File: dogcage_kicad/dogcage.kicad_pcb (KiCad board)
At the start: 2 copper layers, 68.6 x 49.8 mm, 17 parts, among them CON1 5V, M1 XBEE, P1 Door, P2 Servo, P3 CONN_01X10, P4 CONN_01X10, P5 CONN_01X14, P7 CONN_01X14, Q1 TIP120, SW1 SW_PUSH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

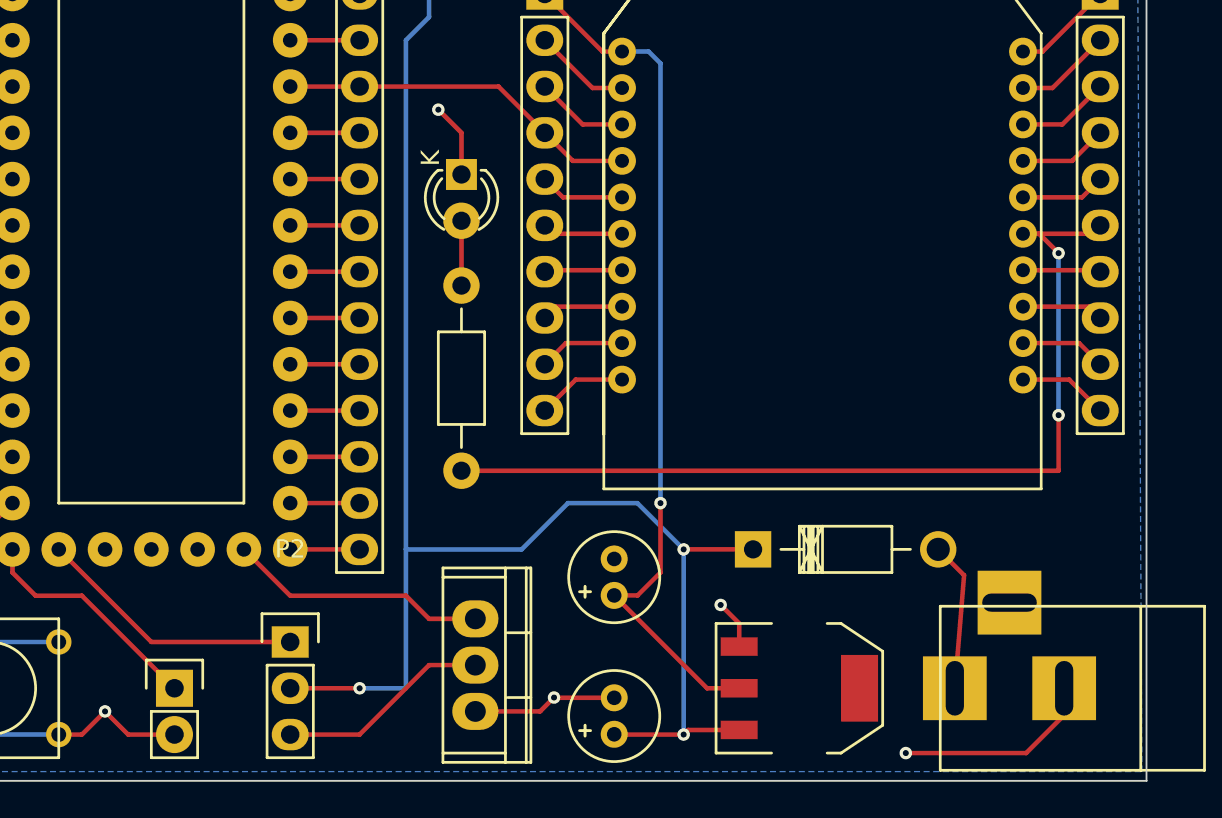
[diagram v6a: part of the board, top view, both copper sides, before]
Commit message: Fixed front silkscreen, added name/email to back
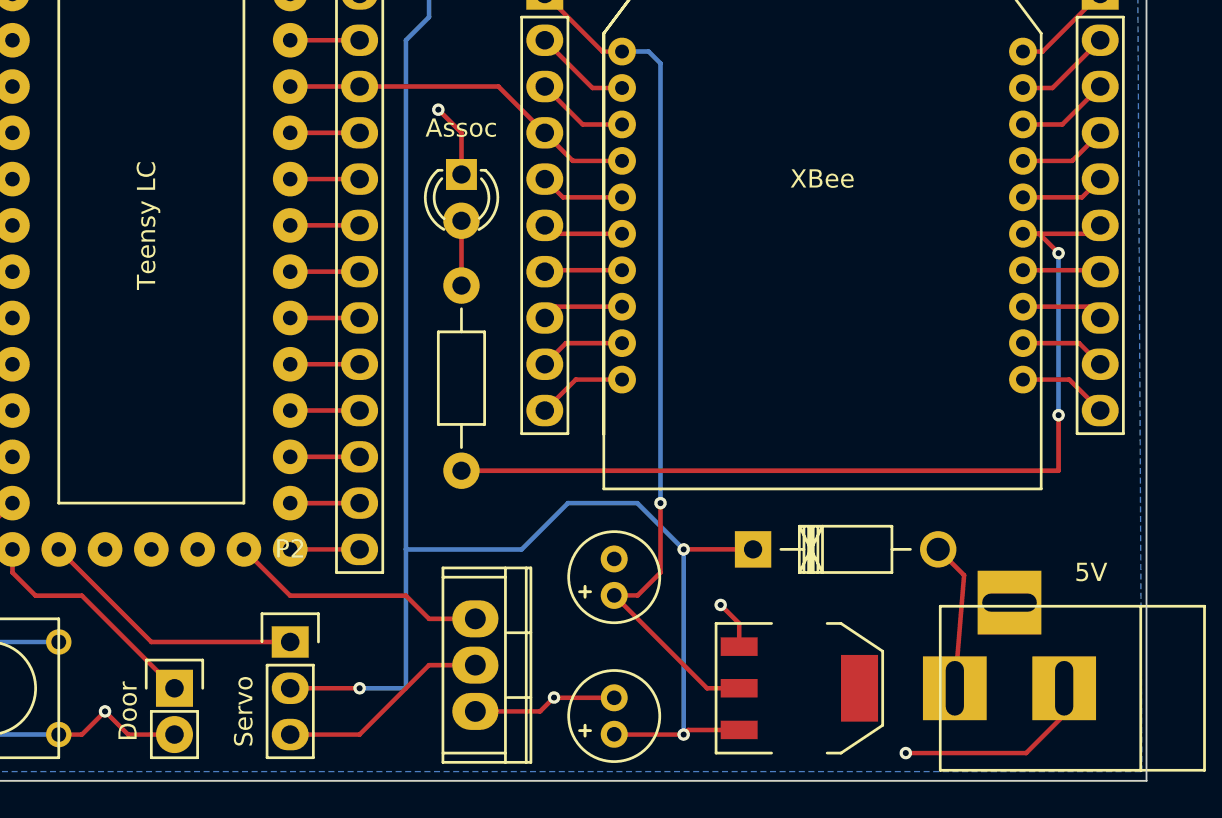
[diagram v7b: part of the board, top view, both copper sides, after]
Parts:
- M1: value XBEE -> XBee
- U2: value TEENSYLC -> Teensy LC
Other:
- board text added: "https://github.com/tpmanley/dogcage Tom Manley tom.manley@gmail.com"
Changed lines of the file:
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@@
     (area 126.971667 123.315 201.577621 175.310001)
     (thickness 1.6)
-    (drawings 4)
+    (drawings 5)
     (tracks 157)
     (zones 0)
@@
     (0 F.Cu signal)
     (31 B.Cu signal)
-    (32 B.Adhes user)
-    (33 F.Adhes user)
-    (34 B.Paste user)
-    (35 F.Paste user)
     (36 B.SilkS user)
     (37 F.SilkS user)
     (38 B.Mask user)
     (39 F.Mask user)
-    (40 Dwgs.User user)
-    (41 Cmts.User user)
-    (42 Eco1.User user)
-    (43 Eco2.User user)
     (44 Edge.Cuts user)
-    (45 Margin user)
-    (46 B.CrtYd user)
-    (47 F.CrtYd user)
-    (48 B.Fab user)
-    (49 F.Fab user)
   )
   (setup
@@
     (visible_elements FFFFFF7F)
     (pcbplotparams
-      (layerselection 0x00030_80000001)
-      (usegerberextensions false)
+      (layerselection 0x010f0_80000001)
+      (usegerberextensions true)
       (excludeedgelayer true)
       (linewidth 0.100000)
@@
       (outputformat 1)
       (mirror false)
-      (drillshape 1)
+      (drillshape 0)
       (scaleselection 1)
-      (outputdirectory ""))
+      (outputdirectory gerbers/))
   )
   (net 0 "")
@@
       (effects (font (size 1 1) (thickness 0.15)))
     )
-    (fp_text value 5V (at -1.27 6.35 180) (layer F.Fab)
+    (fp_text value 5V (at -1.27 6.35 180) (layer F.SilkS)
       (effects (font (size 1 1) (thickness 0.15)))
     )
@@
       (effects (font (size 1 1) (thickness 0.15)))
     )
-    (fp_text value Assoc (at -2.54 0 360) (layer F.Fab)
+    (fp_text value Assoc (at -2.54 0 360) (layer F.SilkS)
       (effects (font (size 1 1) (thickness 0.15)))
     )
@@
     (fp_arc (start 1.28 0) (end 3.02 0.96) (angle 110) (layer F.SilkS) (width 0.15))
     (fp_arc (start 1.27 0) (end 2.44 0.94) (angle 95.5) (layer F.SilkS) (width 0.15))
-    (fp_text user K (at -0.9 1.7 270) (layer F.SilkS)
+    (fp_text user K (at -0.9 1.7 270) (layer F.SilkS) hide
       (effects (font (size 1 1) (thickness 0.15)))
     )
@@
       (effects (font (size 1 1) (thickness 0.15)))
     )
-    (fp_text value XBEE (at 0 0) (layer F.Fab) hide
+    (fp_text value XBee (at 0 0) (layer F.SilkS)
       (effects (font (size 1 1) (thickness 0.15)))
     )
@@
       (effects (font (size 1 1) (thickness 0.15)))
     )
-    (fp_text value Door (at -2.54 1.27 90) (layer F.Fab)
+    (fp_text value Door (at -2.54 1.27 90) (layer F.SilkS)
       (effects (font (size 1 1) (thickness 0.15)))
     )
@@
       (effects (font (size 1 1) (thickness 0.15)))
     )
-    (fp_text value Servo (at -2.54 3.81 90) (layer F.Fab)
+    (fp_text value Servo (at -2.54 3.81 90) (layer F.SilkS)
       (effects (font (size 1 1) (thickness 0.15)))
     )
@@
     (fp_line (start 2.032 -4.572) (end 3.556 -2.286) (layer F.SilkS) (width 0.15))
     (fp_line (start 3.556 -2.286) (end 3.556 -1.524) (layer F.SilkS) (width 0.15))
-    (pad 4 smd rect (at 0 -3.302 270) (size 3.6576 2.032) (layers F.Cu F.Paste F.Mask))
-    (pad 2 smd rect (at 0 3.302 270) (size 1.016 2.032) (layers F.Cu F.Paste F.Mask)
+    (pad 4 smd rect (at 0 -3.302 270) (size 3.6576 2.032) (layers F.Cu F.Mask))
+    (pad 2 smd rect (at 0 3.302 270) (size 1.016 2.032) (layers F.Cu F.Mask)
       (net 3 +3V3))
-    (pad 3 smd rect (at 2.286 3.302 270) (size 1.016 2.032) (layers F.Cu F.Paste F.Mask)
+    (pad 3 smd rect (at 2.286 3.302 270) (size 1.016 2.032) (layers F.Cu F.Mask)
       (net 1 +5V))
-    (pad 1 smd rect (at -2.286 3.302 270) (size 1.016 2.032) (layers F.Cu F.Paste F.Mask)
+    (pad 1 smd rect (at -2.286 3.302 270) (size 1.016 2.032) (layers F.Cu F.Mask)
       (net 2 GND))
     (model SMD_Packages.3dshapes/SOT-223.wrl
@@
       (effects (font (size 1.5 1.5) (thickness 0.15)))
     )
-    (fp_text value TEENSYLC (at 5.08 -10.16 270) (layer F.Fab)
-      (effects (font (size 1.5 1.5) (thickness 0.15)))
+    (fp_text value "Teensy LC" (at 12.7 -7.366 270) (layer F.SilkS)
+      (effects (font (size 1 1) (thickness 0.15)))
     )
     (fp_line (start -2.54 -12.7) (end 27.94 -12.7) (layer F.SilkS) (width 0.15))
@@
       (net 2 GND))
   )
+  (gr_text "https://github.com/tpmanley/dogcage\n\nTom Manley\ntom.manley@gmail.com\n" (at 192.532 129.54) (layer B.SilkS)
+    (effects (font (size 1 1) (thickness 0.25)) (justify left mirror))
+  )
   (gr_line (start 198.12 125.476) (end 198.12 175.26) (angle 90) (layer Edge.Cuts) (width 0.1))
   (gr_line (start 129.54 125.476) (end 129.54 175.26) (angle 90) (layer Edge.Cuts) (width 0.1))
@@
   (segment (start 172.72 162.56) (end 172.72 172.72) (width 0.25) (layer B.Cu) (net 1))
   (segment (start 172.72 172.72) (end 168.92524 172.72) (width 0.25) (layer F.Cu) (net 1) (status 20))
-  (segment (start 160.528 141.986) (end 160.528 139.7) (width 0.254) (layer F.Cu) (net 2) (status 400000))
+  (segment (start 160.528 141.986) (end 160.528 139.7) (width 0.254) (layer F.Cu) (net 2))
   (via (at 159.258 138.43) (size 0.6858) (layers F.Cu B.Cu) (net 2))
   (segment (start 160.528 139.7) (end 159.258 138.43) (width 0.254) (layer F.Cu) (net 2))
@@
   (segment (start 195.5 147.24) (end 195.58 147.32) (width 0.25) (layer F.Cu) (net 13) (status 30))
   (segment (start 191.34 147.24) (end 195.5 147.24) (width 0.25) (layer F.Cu) (net 13) (status 30))
-  (segment (start 160.528 158.242) (end 193.294 158.242) (width 0.254) (layer F.Cu) (net 14) (status 400000))
-  (segment (start 192.23 145.24) (end 191.34 145.24) (width 0.254) (layer F.Cu) (net 14) (status 800000))
+  (segment (start 160.528 158.242) (end 193.294 158.242) (width 0.254) (layer F.Cu) (net 14))
+  (segment (start 192.23 145.24) (end 191.34 145.24) (width 0.254) (layer F.Cu) (net 14))
   (segment (start 193.294 146.304) (end 192.23 145.24) (width 0.254) (layer F.Cu) (net 14))
   (via (at 193.294 146.304) (size 0.6858) (layers F.Cu B.Cu) (net 14))
@@
   (segment (start 151.13 157.48) (end 154.94 157.48) (width 0.25) (layer F.Cu) (net 43) (status 30))
   (segment (start 151.13 160.02) (end 154.94 160.02) (width 0.25) (layer F.Cu) (net 44) (status 30))
-  (segment (start 160.528 144.526) (end 160.528 148.082) (width 0.254) (layer F.Cu) (net 45) (status C00000))
+  (segment (start 160.528 144.526) (end 160.528 148.082) (width 0.254) (layer F.Cu) (net 45))
   (segment (start 151.13 137.16) (end 154.94 137.16) (width 0.25) (layer F.Cu) (net 46) (status 30))
   (segment (start 162.56 137.16) (end 165.1 139.7) (width 0.25) (layer F.Cu) (net 46) (status 20))
